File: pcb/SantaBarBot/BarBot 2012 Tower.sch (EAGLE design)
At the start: 49 parts, among them J1 AVR_SPI_PRG_62X3_LOCK, J2 POWER_JACKSLT, U1 ATMEGA328P, U2 L298_BRIDGE_DRIVER, U3 742G04DBVR, U5 LMV324IDR, U6 SN75HVD179D

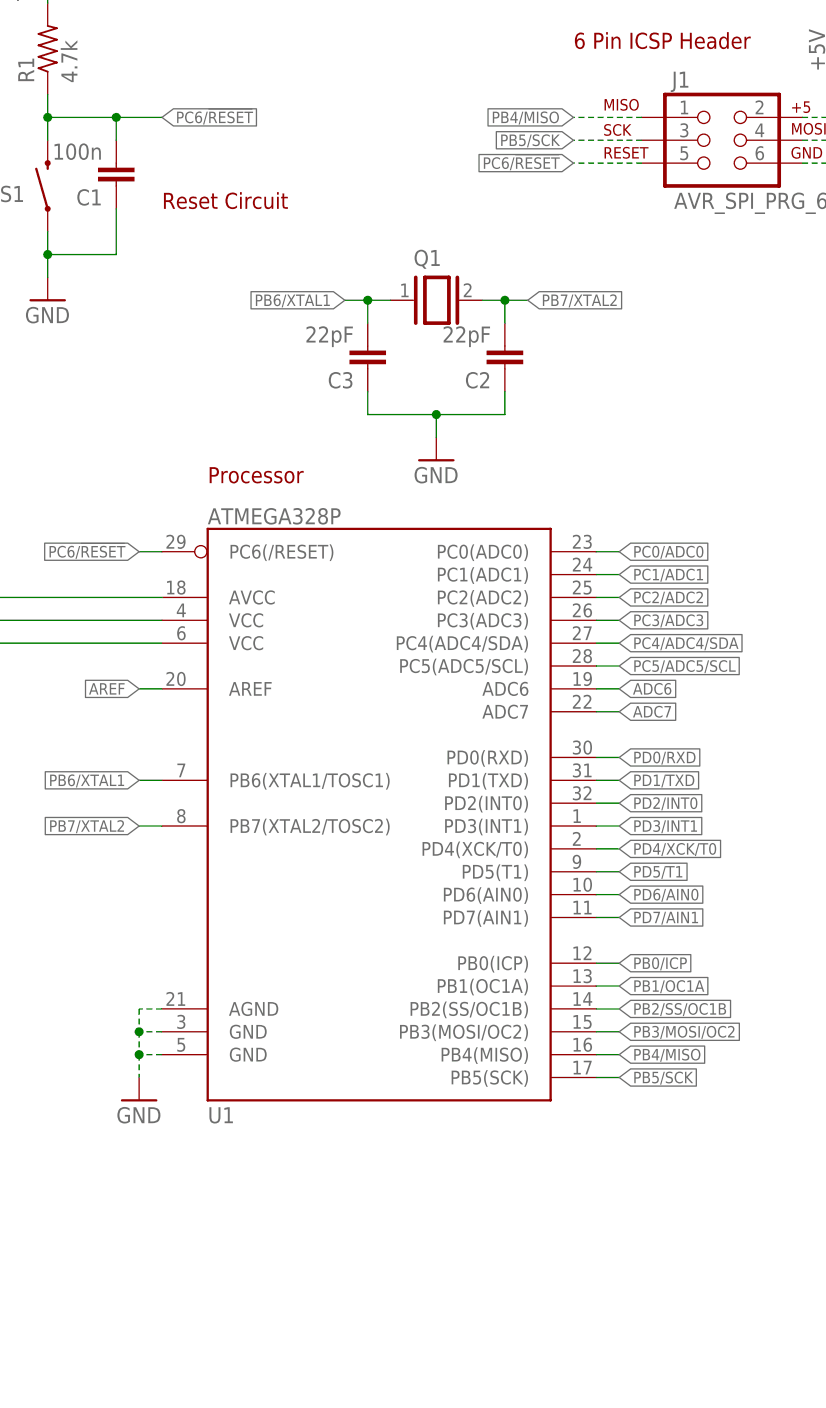
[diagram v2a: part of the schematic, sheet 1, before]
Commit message: Changed board to 2 layers, 3x3 inches.  Fully routed, DRC and ERC run, all errors corrected.  PDFs generated
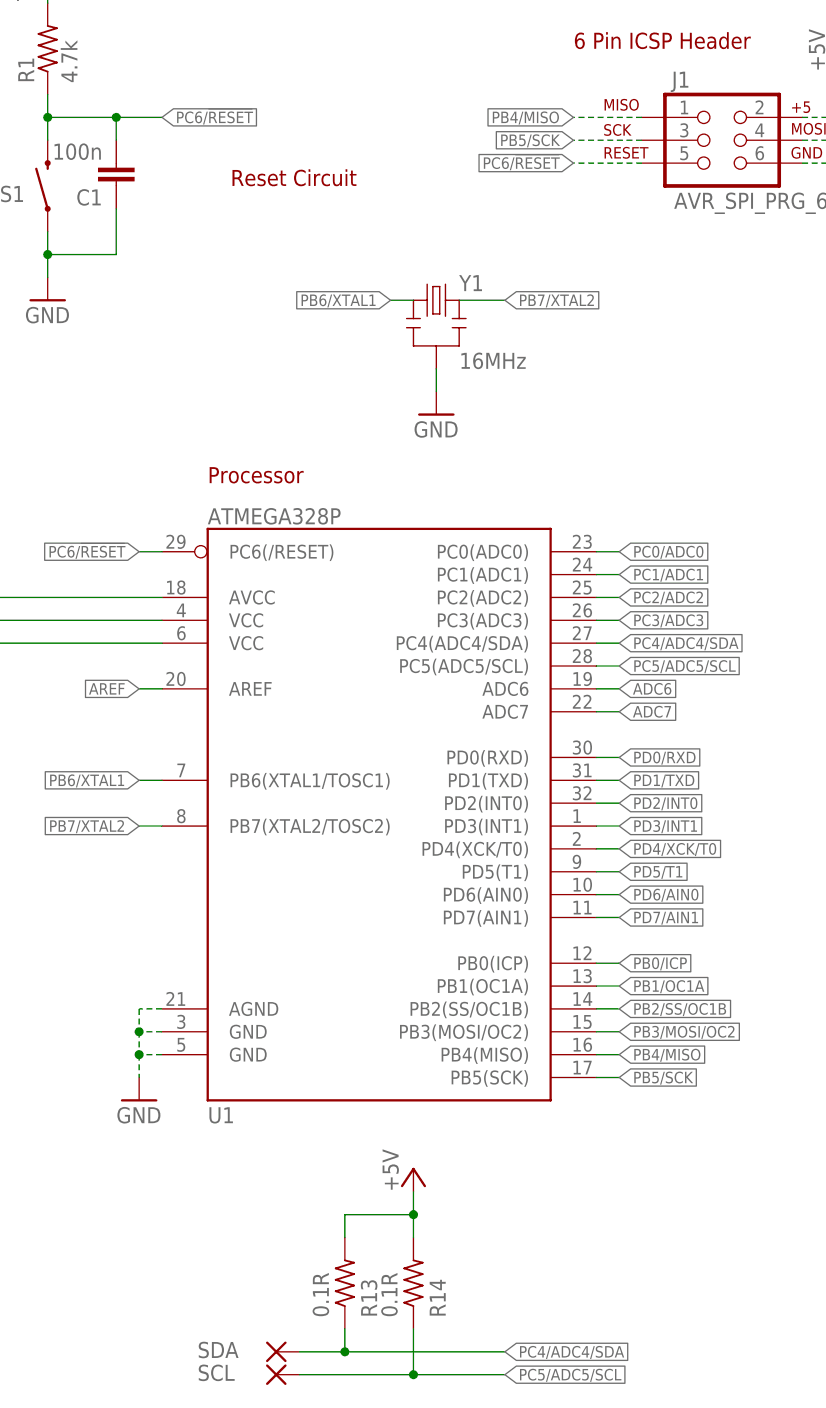
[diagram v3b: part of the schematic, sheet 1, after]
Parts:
- removed C2, C3: 22pF, rcl:C-EUC0603
- removed L1: (no value), wuerth-elektronik:WE-CBF_0805
- removed Q1: (no value), special:XTAL/S
- added R13, R14: 0.1R, rcl:R-US_R2012
- added SCL, SDA: (no value), wirepad:1,6/0,8
- added Y1: 16MHz, SparkFun-FreqCtrl:RESONATOR16MHZ
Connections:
- removed net GNDA: C4.1, D2.A, D4.A, D6.A, D8.A, J2.GND, J2.GNDBREAK, JP2.4, L1.2, R4.1, R5.1
- net +5V: now also R13.2, R14.2
- net GND: now also C4.1, D2.A, D4.A, D6.A, D8.A, J2.GND, J2.GNDBREAK, JP2.4, R4.1, R5.1, Y1.2; no longer C2.1, C3.1, L1.1
- net PB6/XTAL1: now also Y1.1; no longer C3.2, Q1.1
- net PB7/XTAL2: now also Y1.3; no longer C2.2, Q1.2
- net PC4/ADC4/SDA: now also R13.1, SDA.P
- net PC5/ADC5/SCL: now also R14.1, SCL.P

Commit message: Added 2nd RJ45 jack, added testpoints for UART, moved silk layer to copper.  Cleaned up a couple things in the schematic.  Removed some testpoints.
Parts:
- removed SCL, SDA, TP10, TP11, TP12, TP13: (no value), wirepad:1,6/0,8
- removed U$1: RJ45-8PTH, SparkFun-Connectors:RJ45-8PTH
- added RX, TX: RJ45-8PTH, SparkFun-Connectors:RJ45-8PTH
- R13, R14: value 0.1R -> 4.7k
- renumbered J1 to ICSP
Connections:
- removed net N$1: TP10.P, U$1.3
- removed net N$2: TP11.P, U$1.4
- removed net N$4: TP12.P, U$1.5
- removed net N$5: TP13.P, U$1.6
- new net RJ_RX_3: RX.3
- new net RJ_RX_4: RX.4
- new net RJ_RX_5: RX.5
- new net RJ_RX_6: RX.6
- new net RJ_RX_7: RX.7
- new net RJ_RX_8: RX.8
- new net RJ_TX_3: TX.3
- new net RJ_TX_4: TX.4
- new net RJ_TX_5: TX.5
- new net RJ_TX_6: TX.6
- new net RJ_TX_7: TX.7
- new net RJ_TX_8: TX.8
- net !RS485_RX: now also RX.2; no longer U$1.8
- net !RS485_TX: now also TX.2; no longer U$1.2
- net PC4/ADC4/SDA: no longer SDA.P
- net PC5/ADC5/SCL: no longer SCL.P
- net RS485_RX: now also RX.1; no longer U$1.7
- net RS485_TX: now also TX.1; no longer U$1.1
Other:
- note added: "AUTHOR: Dan Kouba"
- moved on the sheet: D1, D2, D3, D4, D5, D6, D7, D8, JP2, M1+, M1-, M2+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

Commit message: Fixed component IDs so they don't violate clearance requirements, made them smaller.  Routed extra opamp to unused ADC pin.
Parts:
- removed PAD3: (no value), wirepad:1,6/0,8
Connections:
- removed net N$7: PAD3.P, R2.1, U5D.OUT
- net ADC6: now also R2.1, U5D.OUT
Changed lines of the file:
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@@
 <grid distance="0.1" unitdist="inch" unit="inch" style="lines" multiple="1" display="no" altdistance="0.01" altunitdist="inch" altunit="inch"/>
 <layers>
-<layer number="1" name="Top" color="4" fill="1" visible="no" active="no"/>
-<layer number="2" name="Route2" color="1" fill="3" visible="no" active="no"/>
-<layer number="15" name="Route15" color="4" fill="6" visible="no" active="no"/>
-<layer number="16" name="Bottom" color="1" fill="1" visible="no" active="no"/>
-<layer number="17" name="Pads" color="2" fill="1" visible="no" active="no"/>
-<layer number="18" name="Vias" color="2" fill="1" visible="no" active="no"/>
-<layer number="19" name="Unrouted" color="6" fill="1" visible="no" active="no"/>
-<layer number="20" name="Dimension" color="15" fill="1" visible="no" active="no"/>
-<layer number="21" name="tPlace" color="7" fill="1" visible="no" active="no"/>
-<layer number="22" name="bPlace" color="7" fill="1" visible="no" active="no"/>
-<layer number="23" name="tOrigins" color="15" fill="1" visible="no" active="no"/>
-<layer number="24" name="bOrigins" color="15" fill="1" visible="no" active="no"/>
-<layer number="25" name="tNames" color="7" fill="1" visible="no" active="no"/>
-<layer number="26" name="bNames" color="7" fill="1" visible="no" active="no"/>
-<layer number="27" name="tValues" color="7" fill="1" visible="no" active="no"/>
-<layer number="28" name="bValues" color="7" fill="1" visible="no" active="no"/>
+<layer number="1" name="Top" color="4" fill="1" visible="yes" active="no"/>
+<layer number="2" name="Route2" color="1" fill="3" visible="yes" active="no"/>
+<layer number="15" name="Route15" color="4" fill="6" visible="yes" active="no"/>
+<layer number="16" name="Bottom" color="1" fill="1" visible="yes" active="no"/>
+<layer number="17" name="Pads" color="2" fill="1" visible="yes" active="no"/>
+<layer number="18" name="Vias" color="2" fill="1" visible="yes" active="no"/>
+<layer number="19" name="Unrouted" color="6" fill="1" visible="yes" active="no"/>
+<layer number="20" name="Dimension" color="15" fill="1" visible="yes" active="no"/>
+<layer number="21" name="tPlace" color="7" fill="1" visible="yes" active="no"/>
+<layer number="22" name="bPlace" color="7" fill="1" visible="yes" active="no"/>
+<layer number="23" name="tOrigins" color="15" fill="1" visible="yes" active="no"/>
+<layer number="24" name="bOrigins" color="15" fill="1" visible="yes" active="no"/>
+<layer number="25" name="tNames" color="7" fill="1" visible="yes" active="no"/>
+<layer number="26" name="bNames" color="7" fill="1" visible="yes" active="no"/>
+<layer number="27" name="tValues" color="7" fill="1" visible="yes" active="no"/>
+<layer number="28" name="bValues" color="7" fill="1" visible="yes" active="no"/>
 <layer number="29" name="tStop" color="7" fill="3" visible="no" active="no"/>
 <layer number="30" name="bStop" color="7" fill="6" visible="no" active="no"/>
@@
 <layer number="35" name="tGlue" color="7" fill="4" visible="no" active="no"/>
 <layer number="36" name="bGlue" color="7" fill="5" visible="no" active="no"/>
-<layer number="37" name="tTest" color="7" fill="1" visible="no" active="no"/>
-<layer number="38" name="bTest" color="7" fill="1" visible="no" active="no"/>
+<layer number="37" name="tTest" color="7" fill="1" visible="yes" active="no"/>
+<layer number="38" name="bTest" color="7" fill="1" visible="yes" active="no"/>
 <layer number="39" name="tKeepout" color="4" fill="11" visible="no" active="no"/>
 <layer number="40" name="bKeepout" color="1" fill="11" visible="no" active="no"/>
@@
 <layer number="44" name="Drills" color="7" fill="1" visible="no" active="no"/>
 <layer number="45" name="Holes" color="7" fill="1" visible="no" active="no"/>
-<layer number="46" name="Milling" color="3" fill="1" visible="no" active="no"/>
-<layer number="47" name="Measures" color="7" fill="1" visible="no" active="no"/>
-<layer number="48" name="Document" color="7" fill="1" visible="no" active="no"/>
-<layer number="49" name="Reference" color="7" fill="1" visible="no" active="no"/>
-<layer number="50" name="dxf" color="7" fill="1" visible="no" active="no"/>
-<layer number="51" name="tDocu" color="7" fill="1" visible="no" active="no"/>
-<layer number="52" name="bDocu" color="7" fill="1" visible="no" active="no"/>
-<layer number="53" name="tGND_GNDA" color="7" fill="9" visible="no" active="no"/>
-<layer number="54" name="bGND_GNDA" color="1" fill="9" visible="no" active="no"/>
-<layer number="56" name="wert" color="7" fill="1" visible="no" active="no"/>
+<layer number="46" name="Milling" color="3" fill="1" visible="yes" active="no"/>
+<layer number="47" name="Measures" color="7" fill="1" visible="yes" active="no"/>
+<layer number="48" name="Document" color="7" fill="1" visible="yes" active="no"/>
+<layer number="49" name="Reference" color="7" fill="1" visible="yes" active="no"/>
+<layer number="50" name="dxf" color="7" fill="1" visible="yes" active="no"/>
+<layer number="51" name="tDocu" color="7" fill="1" visible="yes" active="no"/>
+<layer number="52" name="bDocu" color="7" fill="1" visible="yes" active="no"/>
+<layer number="53" name="tGND_GNDA" color="7" fill="9" visible="yes" active="no"/>
+<layer number="54" name="bGND_GNDA" color="1" fill="9" visible="yes" active="no"/>
+<layer number="56" name="wert" color="7" fill="1" visible="yes" active="no"/>
 <layer number="91" name="Nets" color="2" fill="1" visible="yes" active="yes"/>
 <layer number="92" name="Busses" color="1" fill="1" visible="yes" active="yes"/>
@@
 <part name="PAD1" library="wirepad" deviceset="1,6/0,8" device=""/>
 <part name="PAD2" library="wirepad" deviceset="1,6/0,8" device=""/>
-<part name="PAD3" library="wirepad" deviceset="1,6/0,8" device=""/>
 <part name="GND7" library="supply1" deviceset="GND" device=""/>
 <part name="M1+" library="wirepad" deviceset="3,81/1,4" device=""/>
@@
 <instance part="PAD1" gate="P" x="116.84" y="53.34"/>
 <instance part="PAD2" gate="P" x="116.84" y="48.26"/>
-<instance part="PAD3" gate="P" x="147.32" y="50.8" smashed="yes" rot="R180">
-<attribute name="NAME" x="148.463" y="54.0258" size="1.778" layer="95" rot="R180"/>
-<attribute name="VALUE" x="148.463" y="54.102" size="1.778" layer="96" rot="R180"/>
-</instance>
 <instance part="GND7" gate="1" x="58.42" y="121.92"/>
 <instance part="GND9" gate="1" x="116.84" y="71.12"/>
@@
 <label x="78.74" y="91.44" size="1.27" layer="95" xref="yes"/>
 </segment>
+<segment>
+<pinref part="U5" gate="D" pin="OUT"/>
+<wire x1="139.7" y1="50.8" x2="142.24" y2="50.8" width="0.1524" layer="91"/>
+<pinref part="R2" gate="G$1" pin="1"/>
+<wire x1="142.24" y1="50.8" x2="144.78" y2="50.8" width="0.1524" layer="91"/>
+<wire x1="137.16" y1="40.64" x2="142.24" y2="40.64" width="0.1524" layer="91"/>
+<wire x1="142.24" y1="40.64" x2="142.24" y2="50.8" width="0.1524" layer="91"/>
+<junction x="142.24" y="50.8"/>
+<label x="144.78" y="50.8" size="1.778" layer="95" xref="yes"/>
+</segment>
 </net>
 <net name="PC4/ADC4/SDA" class="0">
@@
 </segment>
 </net>
-<net name="N$7" class="0">
-<segment>
-<pinref part="U5" gate="D" pin="OUT"/>
-<wire x1="139.7" y1="50.8" x2="142.24" y2="50.8" width="0.1524" layer="91"/>
-<pinref part="R2" gate="G$1" pin="1"/>
-<wire x1="142.24" y1="50.8" x2="144.78" y2="50.8" width="0.1524" layer="91"/>
-<wire x1="137.16" y1="40.64" x2="142.24" y2="40.64" width="0.1524" layer="91"/>
-<wire x1="142.24" y1="40.64" x2="142.24" y2="50.8" width="0.1524" layer="91"/>
-<junction x="142.24" y="50.8"/>
-<pinref part="PAD3" gate="P" pin="P"/>
-</segment>
-</net>

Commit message: Board ready for review.  Rendered in 3D, see board_render.png.  Netlist/pinlist/partlist/pdfs updated
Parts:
- removed U6: SN75HVD179D, texas:SN75HVD179D
- added C2, C3: 100n, rcl:C-EUC0805
- added LED1, LED2, LED3: (no value), led:LEDCHIPLED_0805
- added R15, R16, R17: 0.1R, rcl:R-US_R0805
- added U4: LMV324IDR, bb_parts_OpAmp:LMV324IDR
- C1, C5: device rcl:C-EUC2012 -> rcl:C-EUC0805
- C4: value 100n -> (none); device rcl:C-EUC2012 -> rcl:CPOL-USE3.5-8
- JP1: device SparkFun-Connectors:USBPTH -> con-berg:PN61729-S
- M1+, M1-, M2+, M2-: device wirepad:3,81/1,4 -> wirepad:3,81/1,1
- R1, R10, R11, R12, R13, R14, R2, R4, R6, R8: device rcl:R-US_R2012 -> rcl:R-US_R0805
- R3: value 120 -> 0.1R; device rcl:R-US_R2012 -> rcl:R-US_R0805; DIGIKEY_PN (none) -> RHM.10MCT-ND
- R5: value 0.1R -> (none); device rcl:R-US_R2012 -> rcl:R-US_R0805; DIGIKEY_PN RHM.10MCT-ND -> (none)
- R7: value (none) -> 4.7k; device rcl:R-US_R2012 -> rcl:R-US_R0805
- R9: value 4.7k -> 120; device rcl:R-US_R2012 -> rcl:R-US_R0805
- U2: value L298_BRIDGE_DRIVER -> SN75HVD179D; device SparkFun-PowerIC:L298_BRIDGE_DRIVER -> texas:SN75HVD179D; DIGIKEY_PN 497-3624-1-ND -> (none)
- U5: value LMV324IDR -> L298; device bb_parts_OpAmp:LMV324IDR -> st-microelectronics:L298
- renumbered JP2 to LED
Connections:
- new net N$2: LED1.A, R15.1
- new net N$4: LED2.A, R16.1
- new net N$5: LED3.A, R17.1
- net !PD4/XCK/T0: now also U5.INPUT2; no longer U2.IN2
- net !PD7/AIN1: now also U5.INPUT4; no longer U2.IN3
- net !RS485_RX: now also U2G$1.B; no longer U6G$1.B
- net !RS485_TX: now also R9.1, U2G$1.Z; no longer R3.1, U6G$1.Z
- net +5V: now also C2.2, JP1.2, R15.2, R16.2, R17.2, R6.2, U2G$2.VCC, U4G$5.+VS, U5.VS; no longer JP1.VBUS, R7.2, U2.VSS, U5G$5.+VS, U6G$2.VCC
- net +5V/2: now also C3.2, C4.+, U5.VCC; no longer C4.2, U2.VS
- net ADC6: now also U4D.OUT; no longer U5D.OUT
- net AREF: now also U4C.-IN, U4C.OUT; no longer U5C.-IN, U5C.OUT
- net GND: now also C2.1, C3.1, C4.-, JP1.3, R3.1, U2G$2.GND, U4G$5.-VS, U5.GND; no longer C4.1, JP1.GND, R6.1, U2.GND@1, U2.GND@10, U2.GND@11, U2.GND@20, U5G$5.-VS, U6G$2.GND
- net M1+: now also U5.OUT1; no longer U2.OUT1
- net M1-: now also U5.OUT2; no longer U2.OUT2
- net M2+: now also U5.OUT4; no longer U2.OUT4
- net M2-: now also U5.OUT3; no longer U2.OUT3
- net N$10: now also R5.2, R6.1, U4C.+IN; no longer R6.2, R7.1, U5C.+IN
- net N$3: now also U4D.-IN; no longer U5D.-IN
- net PB0/ICP: now also LED1.C
- net PB1/OC1A: now also LED2.C
- net PB2/SS/OC1B: now also LED3.C
- net PB4/MISO: now also R7.1; no longer R8.1
- net PB5/SCK: now also R8.1; no longer R9.1
- net PC0/ADC0: now also U4A.-IN, U4A.OUT; no longer U5A.-IN, U5A.OUT
- net PC1/ADC1: now also U4B.-IN, U4B.OUT; no longer U5B.-IN, U5B.OUT
- net PD0/RXD: now also U2G$1.R; no longer U6G$1.R
- net PD1/TXD: now also U2G$1.D; no longer U6G$1.D
- net PD4/XCK/T0: now also U5.INPUT1; no longer U2.IN1
- net PD5/T1: now also U5.ENABLE_A; no longer U2.ENA
- net PD6/AIN0: now also U5.ENABLE_B; no longer U2.ENB
- net PD7/AIN1: now also U5.INPUT3; no longer U2.IN4
- net RS485_RX: now also U2G$1.A; no longer U6G$1.A
- net RS485_TX: now also R9.2, U2G$1.Y; no longer R3.2, U6G$1.Y
- net SENSE_A: now also R3.2, U4A.+IN, U5.SEN_A; no longer R4.2, U2.SENSE_A, U5A.+IN
- net SENSE_B: now also R4.2, U4B.+IN, U5.SEN_B; no longer R5.2, U2.SENSE_B, U5B.+IN
- net SPI_MISO: now also R7.2; no longer R8.2
- net SPI_SCK: now also R8.2; no longer R9.2
- net TP1: now also U4D.+IN; no longer U5D.+IN
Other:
- moved on the sheet: R13, R14, R4, R5, R6, R8, R9
